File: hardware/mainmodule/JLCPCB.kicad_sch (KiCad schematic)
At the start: 63 parts, among them J1 USB+, J10 Conn_01x04, J2 To LED_MOD_0, J3 To EXT_MOD_1, J4 V24_IN, J5 Temp, J6 Presence, J7 Neo, J8 AUX, J9 Conn_01x04, Q1 Si3456DDV, Q2 Si3456DDV, Q3 Si3456DDV, Q4 Si3456DDV, Q5 Si3456DDV, Q6 Si3456DDV, SW1 SW_Push, SW2 SW_Push, U1 ESP32-C6-WROOM-1, U3 74HCT244, U4 DS18B20, U5 MC34063AD

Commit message: Larger resistor footprints, includes some other property updates.
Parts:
- R11, R15: footprint Resistor_SMD:R_0201_0603Metric -> Resistor_SMD:R_0603_1608Metric
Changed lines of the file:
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@@
       (effects (font (size 1.27 1.27)))
     )
-    (property "Footprint" "Resistor_SMD:R_0201_0603Metric" (at 61.595 193.04 0)
+    (property "Footprint" "Resistor_SMD:R_0603_1608Metric" (at 61.595 193.04 0)
       (effects (font (size 1.27 1.27)) hide)
     )
@@
       (effects (font (size 1.27 1.27)))
     )
-    (property "Footprint" "Resistor_SMD:R_0201_0603Metric" (at 41.91 64.77 0)
-      (effects (font (size 1.27 1.27)) hide)
-    )
+    (property "Footprint" "Resistor_SMD:R_0603_1608Metric" (at 41.91 64.77 0)
+      (effects (font (size 1.27 1.27)) hide)
+    )

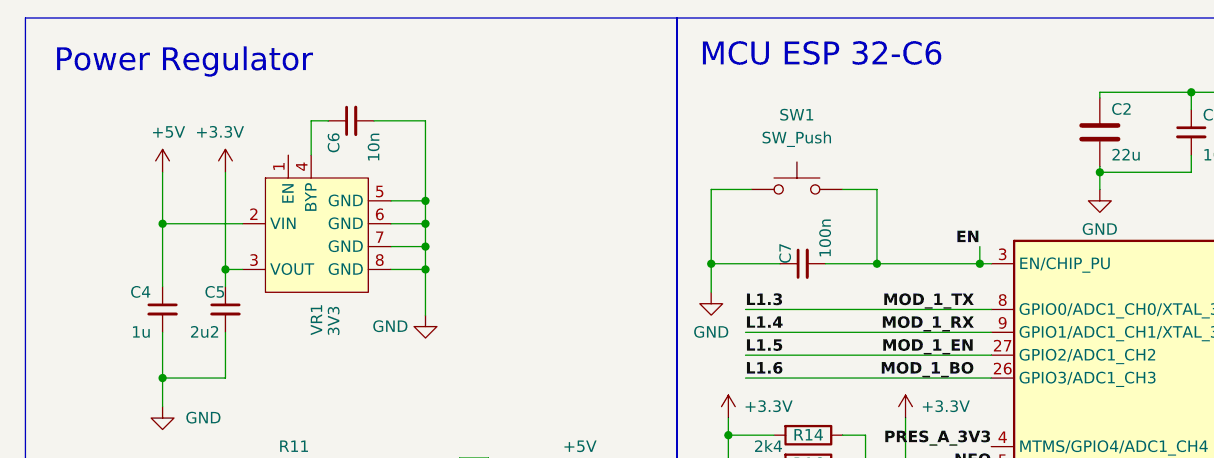
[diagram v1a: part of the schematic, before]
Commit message: Add two missing EN lines.
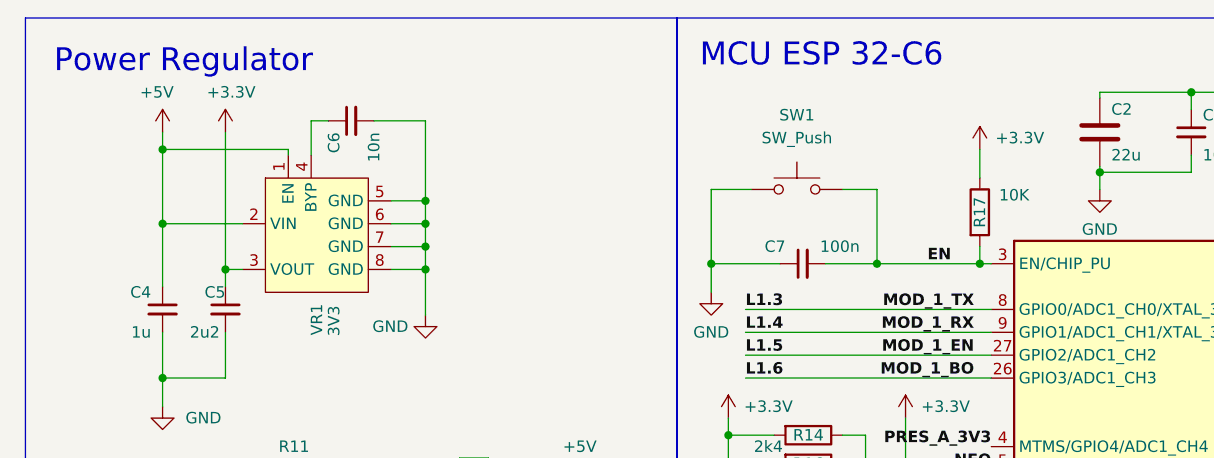
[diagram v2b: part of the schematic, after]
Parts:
- added R17: 10K, Resistor_SMD:R_0603_1608Metric, symbol Device:R
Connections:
- net +3.3V: now also R17.1
- net +5V: now also VR1.1 (EN)
- net EN: now also R17.2
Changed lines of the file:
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@@
   (junction (at 178.435 126.365) (diameter 0) (color 0 0 0 0)
   )
+  (junction (at 27.305 26.67) (diameter 0) (color 0 0 0 0)
+  )
   (junction (at 131.445 29.21) (diameter 0) (color 0 0 0 0)
   )
@@
     (stroke (width 0) (type default))
   )
+  (wire (pts (xy 41.275 26.67) (xy 41.275 27.305))
+    (stroke (width 0) (type default))
+  )
   (wire (pts (xy 227.965 56.515) (xy 227.965 55.245))
     (stroke (width 0) (type default))
@@
     (stroke (width 0) (type default))
   )
+  (wire (pts (xy 27.305 26.67) (xy 27.305 34.925))
+    (stroke (width 0) (type default))
+  )
   (wire (pts (xy 106.68 31.115) (xy 106.68 39.37))
     (stroke (width 0) (type default))
@@
     (stroke (width 0) (type default))
   )
+  (wire (pts (xy 27.305 26.67) (xy 41.275 26.67))
+    (stroke (width 0) (type default))
+  )
   (wire (pts (xy 154.305 141.605) (xy 154.305 170.815))
     (stroke (width 0) (type default))
   )
+  (wire (pts (xy 118.11 26.67) (xy 118.11 29.845))
+    (stroke (width 0) (type default))
+  )
   (wire (pts (xy 215.9 61.595) (xy 232.41 61.595))
     (stroke (width 0) (type default))
@@
     (stroke (width 0) (type default))
   )
-  (wire (pts (xy 34.29 29.21) (xy 34.29 40.005))
-    (stroke (width 0) (type default))
-  )
   (wire (pts (xy 52.705 32.385) (xy 56.515 32.385))
     (stroke (width 0) (type default))
@@
     (stroke (width 0) (type default))
   )
-  (wire (pts (xy 27.305 29.21) (xy 27.305 34.925))
+  (wire (pts (xy 27.305 24.765) (xy 27.305 26.67))
     (stroke (width 0) (type default))
   )
@@
     (stroke (width 0) (type default))
   )
+  (wire (pts (xy 34.29 24.765) (xy 34.29 40.005))
+    (stroke (width 0) (type default))
+  )
   (wire (pts (xy 63.5 62.865) (xy 63.5 60.96))
     (stroke (width 0) (type default))
@@
     (effects (font (size 1.27 1.27) bold) (justify left bottom))
   )
-  (label "EN" (at 118.11 37.465 180) (fields_autoplaced)
+  (label "EN" (at 114.935 39.37 180) (fields_autoplaced)
     (effects (font (size 1.27 1.27) bold) (justify right bottom))
   )
@@
     )
   )
+  (symbol (lib_id "power:+3.3V") (at 118.11 26.67 0) (unit 1)
+    (in_bom yes) (on_board yes) (dnp no)
+    (property "Reference" "#PWR049" (at 118.11 30.48 0)
+      (effects (font (size 1.27 1.27)) hide)
+    )
+    (property "Value" "+3.3V" (at 122.555 25.4 0)
+      (effects (font (size 1.27 1.27)))
+    )
+    (property "Footprint" "" (at 118.11 26.67 0)
+      (effects (font (size 1.27 1.27)) hide)
+    )
+    (property "Datasheet" "" (at 118.11 26.67 0)
+      (effects (font (size 1.27 1.27)) hide)
+    )
+    (pin "1")
+    (instances
+      (project "JLCPCB"
+        (path "/366c4e60-fc00-4520-9ea0-7840d623b51d"
+          (reference "#PWR049") (unit 1)
+        )
+      )
+    )
+  )
   (symbol (lib_id "power:GND") (at 73.025 113.03 0) (unit 1)
     (in_bom yes) (on_board yes) (dnp no) (fields_autoplaced)
@@
   (symbol (lib_id "Device:C_Small") (at 98.425 39.37 90) (unit 1)
     (in_bom yes) (on_board yes) (dnp no)
-    (property "Reference" "C7" (at 96.52 39.37 0)
+    (property "Reference" "C7" (at 96.52 37.465 90)
       (effects (font (size 1.27 1.27)) (justify left))
     )
-    (property "Value" "100n" (at 100.965 38.735 0)
+    (property "Value" "100n" (at 104.775 37.465 90)
       (effects (font (size 1.27 1.27)) (justify left))
     )
@@
     )
   )
+  (symbol (lib_id "Device:R") (at 118.11 33.655 0) (unit 1)
+    (in_bom yes) (on_board yes) (dnp no)
+    (property "Reference" "R17" (at 118.11 33.655 90)
+      (effects (font (size 1.27 1.27)))
+    )
+    (property "Value" "10K" (at 121.92 31.75 0)
+      (effects (font (size 1.27 1.27)))
+    )
+    (property "Footprint" "Resistor_SMD:R_0603_1608Metric" (at 116.332 33.655 90)
+      (effects (font (size 1.27 1.27)) hide)
+    )
+    (property "Datasheet" "~" (at 118.11 33.655 0)
+      (effects (font (size 1.27 1.27)) hide)
+    )
+    (property "Tolerance" "1%" (at 118.11 33.655 90)
+      (effects (font (size 1.27 1.27)) hide)
+    )
+    (property "LCSC" "C23192" (at 118.11 33.655 0)
+      (effects (font (size 1.27 1.27)) hide)
+    )
+    (pin "1")
+    (pin "2")
+    (instances
+      (project "JLCPCB"
+        (path "/366c4e60-fc00-4520-9ea0-7840d623b51d"
+          (reference "R17") (unit 1)
+        )
+      )
+    )
+  )
   (symbol (lib_id "power:GND") (at 92.71 99.695 0) (unit 1)
     (in_bom yes) (on_board yes) (dnp no) (fields_autoplaced)
@@
     )
   )
-  (symbol (lib_id "power:+5V") (at 27.305 29.21 0) (mirror y) (unit 1)
+  (symbol (lib_id "power:+5V") (at 27.305 24.765 0) (unit 1)
     (in_bom yes) (on_board yes) (dnp no)
-    (property "Reference" "#PWR08" (at 27.305 33.02 0)
+    (property "Reference" "#PWR08" (at 27.305 28.575 0)
       (effects (font (size 1.27 1.27)) hide)
     )
-    (property "Value" "+5V" (at 27.94 24.765 0)
+    (property "Value" "+5V" (at 26.67 20.32 0)
       (effects (font (size 1.27 1.27)))
     )
-    (property "Footprint" "" (at 27.305 29.21 0)
+    (property "Footprint" "" (at 27.305 24.765 0)
       (effects (font (size 1.27 1.27)) hide)
     )
-    (property "Datasheet" "" (at 27.305 29.21 0)
+    (property "Datasheet" "" (at 27.305 24.765 0)
       (effects (font (size 1.27 1.27)) hide)
     )
@@
     )
   )
-  (symbol (lib_id "power:+3.3V") (at 34.29 29.21 0) (mirror y) (unit 1)
+  (symbol (lib_id "power:+3.3V") (at 34.29 24.765 0) (unit 1)
     (in_bom yes) (on_board yes) (dnp no)
-    (property "Reference" "#PWR09" (at 34.29 33.02 0)
+    (property "Reference" "#PWR09" (at 34.29 28.575 0)
       (effects (font (size 1.27 1.27)) hide)
     )
-    (property "Value" "+3.3V" (at 33.655 24.765 0)
+    (property "Value" "+3.3V" (at 34.925 20.32 0)
       (effects (font (size 1.27 1.27)))
     )
-    (property "Footprint" "" (at 34.29 29.21 0)
+    (property "Footprint" "" (at 34.29 24.765 0)
       (effects (font (size 1.27 1.27)) hide)
     )
-    (property "Datasheet" "" (at 34.29 29.21 0)
+    (property "Datasheet" "" (at 34.29 24.765 0)
       (effects (font (size 1.27 1.27)) hide)
     )

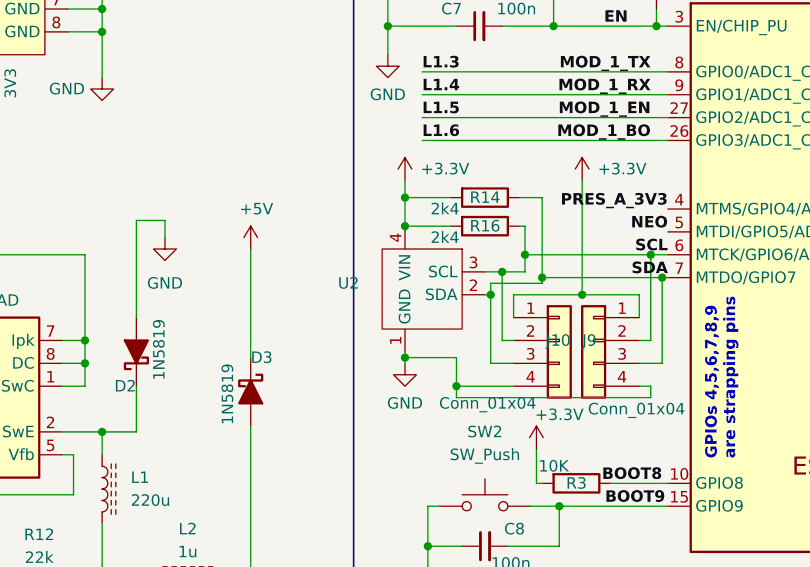
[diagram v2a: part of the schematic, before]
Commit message: Add missing light sensor.
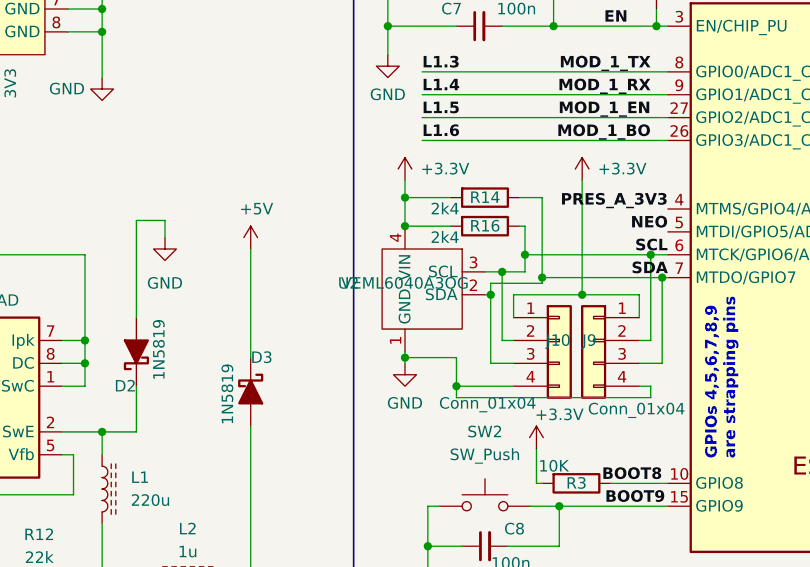
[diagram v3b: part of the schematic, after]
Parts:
- U2: value ~ -> VEML6040A3OG; LCSC (none) -> C78465
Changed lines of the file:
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@@
       (effects (font (size 1.27 1.27)) (justify left))
     )
-    (property "Value" "~" (at 90.17 67.945 0)
+    (property "Value" "VEML6040A3OG" (at 90.17 67.945 0)
       (effects (font (size 1.27 1.27)))
     )
@@
       (effects (font (size 1.27 1.27)) hide)
     )
+    (property "LCSC" "C78465" (at 90.17 67.945 0)
+      (effects (font (size 1.27 1.27)) hide)
+    )

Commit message: Bigger mounting holes (for M3 screws) and less disconnected ground planes.
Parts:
- H1: footprint MountingHole:MountingHole_2.5mm -> MountingHole:MountingHole_3.2mm_M3
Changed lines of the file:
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@@
       (effects (font (size 1.27 1.27)) (justify left))
     )
-    (property "Footprint" "MountingHole:MountingHole_2.5mm" (at 88.9 115.57 0)
+    (property "Footprint" "MountingHole:MountingHole_3.2mm_M3" (at 88.9 115.57 0)
       (effects (font (size 1.27 1.27)) hide)
     )

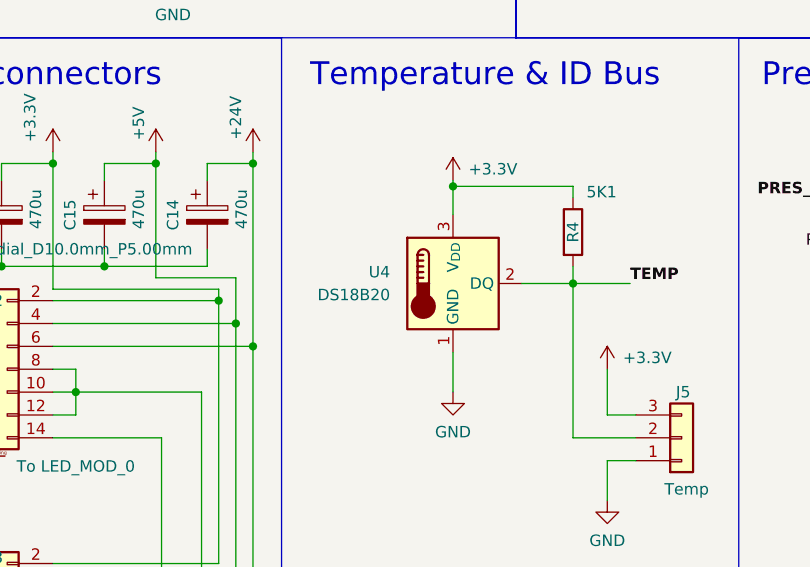
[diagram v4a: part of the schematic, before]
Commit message: Use SMD version of the temperature sensor.
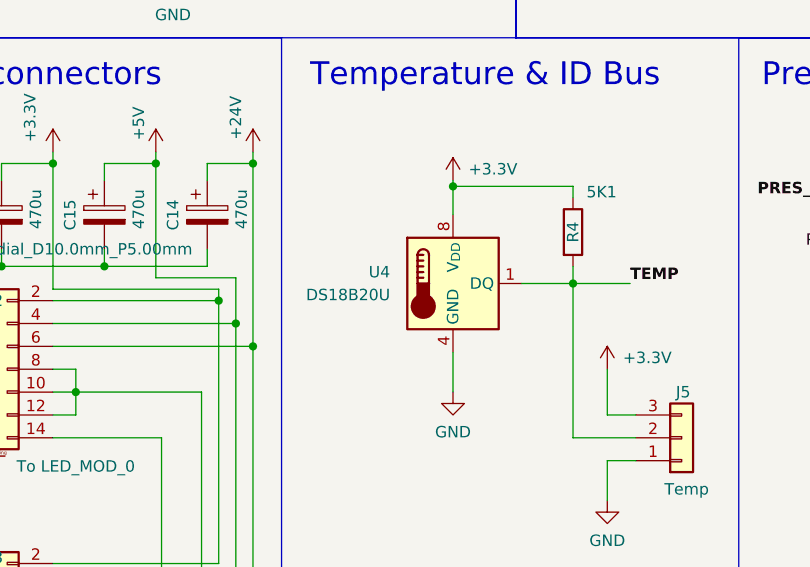
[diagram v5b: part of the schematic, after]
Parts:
- U4: value DS18B20 -> DS18B20U; footprint Package_TO_SOT_THT:TO-92_Inline -> Package_SO:MSOP-8_3x3mm_P0.65mm; symbol Sensor_Temperature:DS18B20 -> Sensor_Temperature:DS18B20U
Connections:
- net +3.3V: now also U4.8 (V_{DD}); no longer U4.3 (V_{DD})
- net GND: now also U4.4 (GND); no longer U4.1 (GND)
- net TEMP: now also U4.1 (DQ); no longer U4.2 (DQ)
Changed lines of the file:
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@@
     )
   )
-  (symbol (lib_id "Sensor_Temperature:DS18B20") (at 178.435 137.16 0) (unit 1)
+  (symbol (lib_id "Sensor_Temperature:DS18B20U") (at 178.435 137.16 0) (unit 1)
     (in_bom yes) (on_board yes) (dnp no) (fields_autoplaced)
     (property "Reference" "U4" (at 171.45 135.89 0)
       (effects (font (size 1.27 1.27)) (justify right))
     )
-    (property "Value" "DS18B20" (at 171.45 138.43 0)
+    (property "Value" "DS18B20U" (at 171.45 138.43 0)
       (effects (font (size 1.27 1.27)) (justify right))
     )
-    (property "Footprint" "Package_TO_SOT_THT:TO-92_Inline" (at 153.035 143.51 0)
+    (property "Footprint" "Package_SO:MSOP-8_3x3mm_P0.65mm" (at 154.305 143.51 0)
       (effects (font (size 1.27 1.27)) hide)
     )
@@
     (pin "2")
     (pin "3")
+    (pin "4")
+    (pin "5")
+    (pin "8")
+    (pin "7")
+    (pin "6")
     (instances
       (project "JLCPCB"
